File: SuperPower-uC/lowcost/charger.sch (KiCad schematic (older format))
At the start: 18 parts, among them J2 Thermistor, Q1 AO3401A, Q2 2N7002, U3 LC709203FQH, U4 TP4056

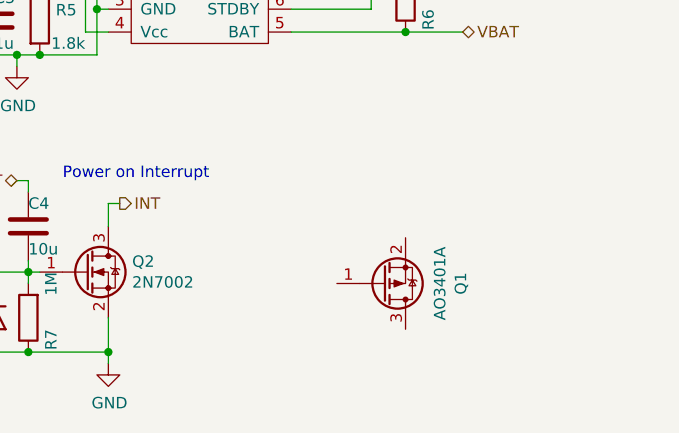
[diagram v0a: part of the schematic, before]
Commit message: fixed annotations
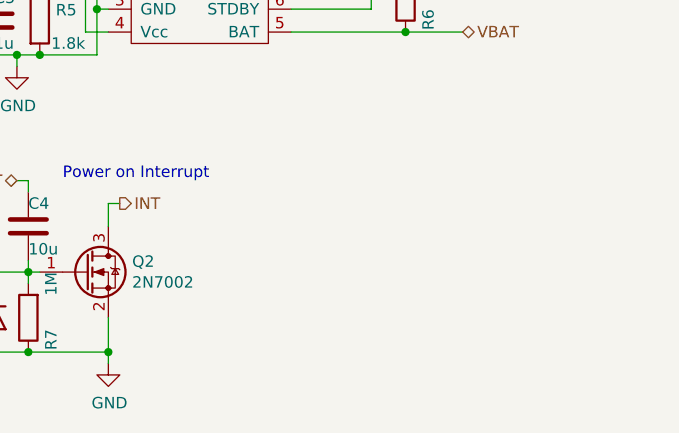
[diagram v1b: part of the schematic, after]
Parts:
- removed Q1: AO3401A, Package_TO_SOT_SMD:SOT-23_Handsoldering, symbol Transistor_FET:AO3401A
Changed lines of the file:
@@
 $EndComp
 $Comp
-L power:GND #PWR?
+L power:GND #PWR0102
 U 1 1 5F833F9C
 P 1500 5150
-F 0 "#PWR?" H 1500 4900 50  0001 C CNN
+F 0 "#PWR0102" H 1500 4900 50  0001 C CNN
 F 1 "GND" H 1505 4977 50  0000 C CNN
 F 2 "" H 1500 5150 50  0001 C CNN
@@
 CHARGE-DISABLE
 $Comp
-L Transistor_FET:AO3401A Q1
-U 1 1 5F8021C7
-P 2700 4800
-F 0 "Q1" V 3042 4800 50  0000 C CNN
-F 1 "AO3401A" V 2951 4800 50  0000 C CNN
-F 2 "Package_TO_SOT_SMD:SOT-23_Handsoldering" H 2900 4725 50  0001 L CIN
-F 3 "http://www.aosmd.com/pdfs/datasheet/AO3401A.pdf" H 2700 4800 50  0001 L CNN
-F 4 "C347476" V 2700 4800 50  0001 C CNN "LCSC"
-	1    2700 4800
-	1    0    0    1
-$EndComp
-$Comp
 L Device:C C3
 U 1 1 5F7FD127
@@
 $EndComp
 $Comp
-L power:GND #PWR?
+L power:GND #PWR0103
 U 1 1 5F7F85B4
 P 1100 3850
-F 0 "#PWR?" H 1100 3600 50  0001 C CNN
+F 0 "#PWR0103" H 1100 3600 50  0001 C CNN
 F 1 "GND" H 1105 3677 50  0000 C CNN
 F 2 "" H 1100 3850 50  0001 C CNN
@@
 	2000 2350 2100 2350
 $Comp
-L power:GND #PWR?
+L power:GND #PWR0104
 U 1 1 5F7EE01C
 P 2100 2350
-F 0 "#PWR?" H 2100 2100 50  0001 C CNN
+F 0 "#PWR0104" H 2100 2100 50  0001 C CNN
 F 1 "GND" H 2105 2177 50  0000 C CNN
 F 2 "" H 2100 2350 50  0001 C CNN
@@
 	950  1350 1200 1350
 $Comp
-L power:GND #PWR?
+L power:GND #PWR0105
 U 1 1 5F7E81F4
 P 950 1350
-F 0 "#PWR?" H 950 1100 50  0001 C CNN
+F 0 "#PWR0105" H 950 1100 50  0001 C CNN
 F 1 "GND" H 955 1177 50  0000 C CNN
 F 2 "" H 950 1350 50  0001 C CNN

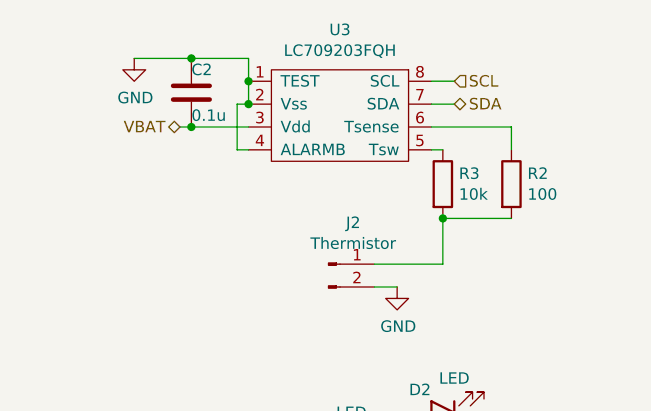
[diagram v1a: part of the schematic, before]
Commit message: fixed erc errors
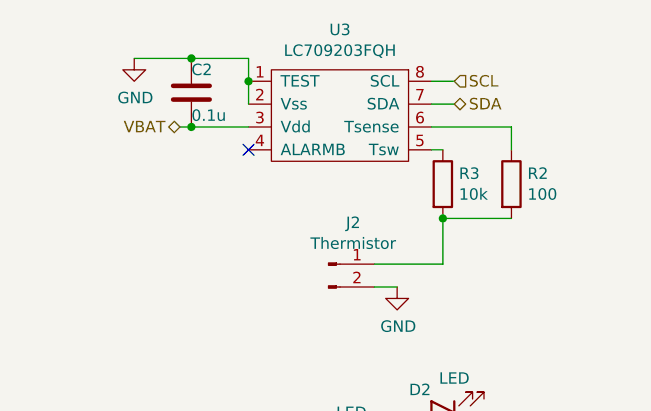
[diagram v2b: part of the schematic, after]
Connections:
- net GND: no longer U3.4 (ALARMB)
- no-connect marks 0 -> 1
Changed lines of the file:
@@
 Text HLabel 900  3300 0    50   Input ~ 0
 VCHARGE
-Wire Wire Line
-	1450 1750 1400 1750
 Text HLabel 1150 1650 0    50   BiDi ~ 0
 VBAT
@@
 Text HLabel 2350 1450 2    50   Input ~ 0
 SCL
-Wire Wire Line
-	1400 1750 1400 1550
-Wire Wire Line
-	1400 1550 1450 1550
-Connection ~ 1450 1550
 Connection ~ 1200 1650
 Wire Wire Line
@@
 Text HLabel 1100 4350 0    50   BiDi ~ 0
 VBAT
+NoConn ~ 1450 1750
 $EndSCHEMATC

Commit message: design rule optimisation
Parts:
- C2: value 0.1u -> 0.1µF
- C3: value 1u -> 1µF
- C4: value 10u -> 10µF
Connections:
- net VCHARGE: no longer D1.2 (A), D2.2 (A), U4.4 (Vcc)
- net STDBY: now reaches R10.2, U4.6 (STDBY)
- net STDBY: now also D1.2 (A), D2.2 (A), U4.4 (Vcc)
- net CHRG: now reaches R4.2, U4.7 (CHRG)
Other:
- moved on the sheet: C3, C4, D1, D2, D3, Q2, R10, R4, R5, R6, R7, U4

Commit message: schematic layout cleaning
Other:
- note added: "Charger\n"
- note added: "Fuel Gauge"
- note added: "Labels\n"
- moved on the sheet: C2, C3, C4, D1, D2, D3, J2, Q2, R10, R2, R3, R4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

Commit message: swapped led and added usb c part number
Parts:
- D1: footprint LED_SMD:LED_0603_1608Metric_Pad1.05x0.95mm_HandSolder -> LED_SMD:LED_0805_2012Metric_Pad1.15x1.40mm_HandSolder; LCSC C2286 -> C84256
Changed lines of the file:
@@
 F 0 "D1" H 6100 4750 50  0000 C CNN
 F 1 "LED" H 5950 4700 50  0000 C CNN
-F 2 "LED_SMD:LED_0603_1608Metric_Pad1.05x0.95mm_HandSolder" H 6000 4850 50  0001 C CNN
+F 2 "LED_SMD:LED_0805_2012Metric_Pad1.15x1.40mm_HandSolder" H 6000 4850 50  0001 C CNN
 F 3 "~" H 6000 4850 50  0001 C CNN
-F 4 "C2286" H 6000 4850 50  0001 C CNN "LCSC"
+F 4 "C84256" H 6000 4850 50  0001 C CNN "LCSC"
 	1    6000 4850
 	-1   0    0    1
